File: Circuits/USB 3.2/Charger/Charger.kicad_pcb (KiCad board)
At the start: 2 copper layers, 7.8 x 7 mm, 1 part

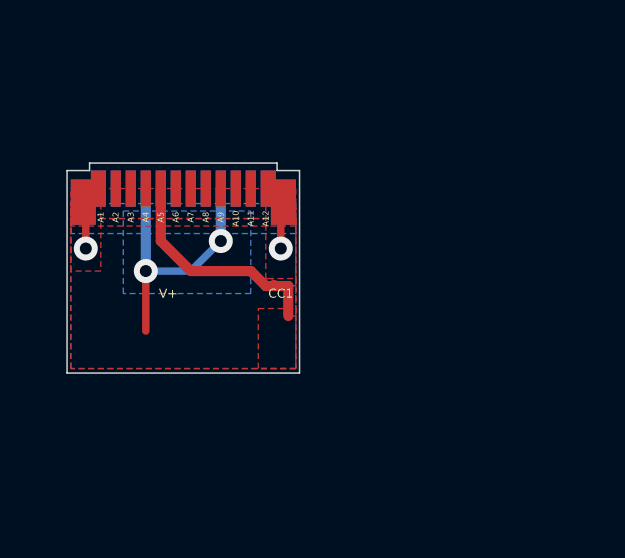
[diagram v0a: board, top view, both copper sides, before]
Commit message: Working on USB 3.2
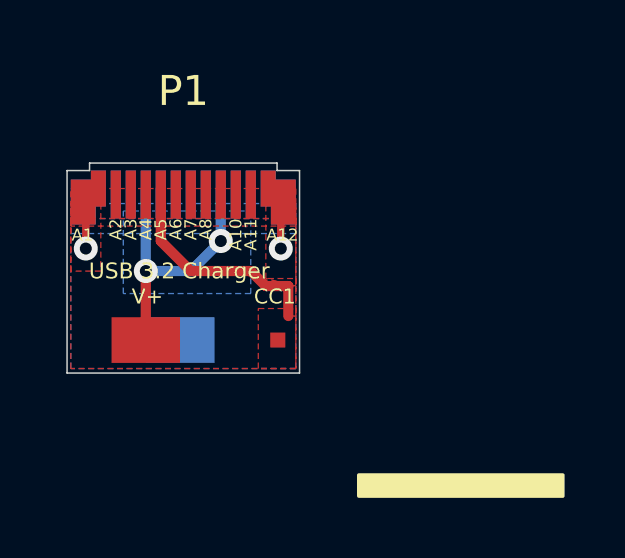
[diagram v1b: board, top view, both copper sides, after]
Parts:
- removed REF**: USB_C_3.2, Footprints:USB_C_3.2
- added P1: USB_C_Plug, Footprints:USB_C_3.2, F.Cu at (149.8, 89.0)
- added W1: V+, Footprints:Pad, F.Cu at (148.5, 94.0)
- added W2: CC1, Footprints:Pad_Small, F.Cu at (152.9, 94.0)
- added W3: GND, Footprints:Pad, B.Cu at (149.7, 94.0)
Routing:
- net Vbus: track 9.41 -> 0.00 mm, vias 2 -> 0
- net /Vbus: track 0.00 -> 9.41 mm, vias 0 -> 2
- net CC1: track 7.62 -> 0.00 mm
- net /CC1: track 0.00 -> 7.62 mm
- net GND: track 4.41 -> 0.00 mm, vias 2 -> 0
- net /GND: track 0.00 -> 4.41 mm, vias 0 -> 2
- added copper zone on F.Cu, net /CC1
- added copper zone on B.Cu, net /GND
- added copper zone on F.Cu, net /GND
- added copper zone on B.Cu, net /Vbus
- added copper zone on F.Cu, net /Vbus
- removed copper zone on F.Cu, net CC1
- removed copper zone on B.Cu, net GND
- removed copper zone on F.Cu, net GND
- removed copper zone on B.Cu, net Vbus
- removed copper zone on F.Cu, net Vbus
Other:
- board text added: "2022.12.03 v1.1"
- board text added: "github.com /Ehryk"
- board text removed: "2022.11.13 v1.0"
- board text removed: "A9"
- board text removed: "B4"
- board text removed: "github.com/Ehryk"
